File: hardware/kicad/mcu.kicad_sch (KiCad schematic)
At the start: 25 parts, among them J3 JST-XH 2p, SW1 RESET, U3 74LVC1G00, U4 74AHCT1G08, U5 74AHCT1G08

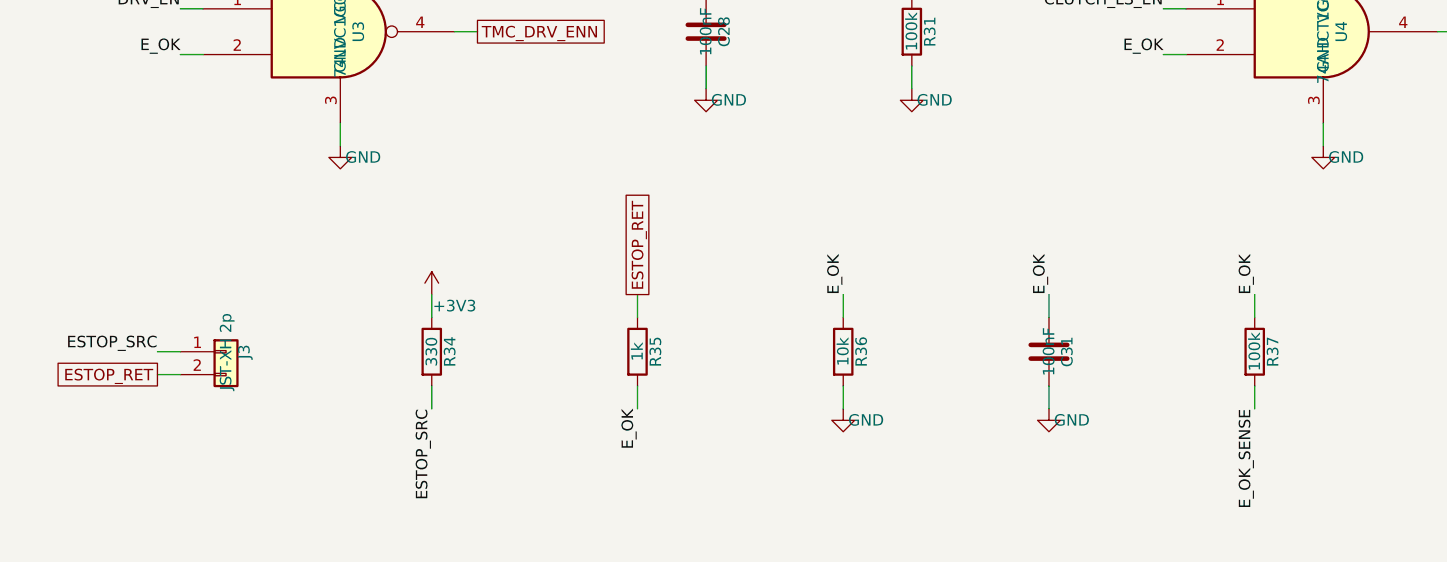
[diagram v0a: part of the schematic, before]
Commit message: Add routed controller PCB, clutch CAD and mill notes
- Schematic: panel ribbon (2x7 IDC) + feed-unit header (JST-XH 7) so all
  connectors fit one 100 mm board edge; fix stub-bridging in the generator.
- PCB (hardware/tools/build_pcb.py): 100x100 mm 4-layer board built from the
  netlist - fixed placement for power/connectors, auto-placed passives,
  GND / split +36V/+3V3 inner planes, Freerouting, post-route power pours,
  GND stitching; fix_planes.py drops plane vias for leftovers;
  check_pcb.py runs DRC with schematic parity. 3D renders in hardware/renders.
  Status: 5 unconnected items + 2 starved thermals left for interactive
  routing (see hardware/kicad/drc.json after check_pcb.py).
- mechanical/clutch: parametric build123d model of the DIY tooth clutch
  (field housing, coil, rotor, armature, leaf springs, output hub/shaft,
  cover), STEP/STL export and VTK renders.
- docs/mill.md: SIEG X3.5D research and the measurements still needed.

Co-Authored-By: Claude Opus 5.5 <noreply@anthropic.com>
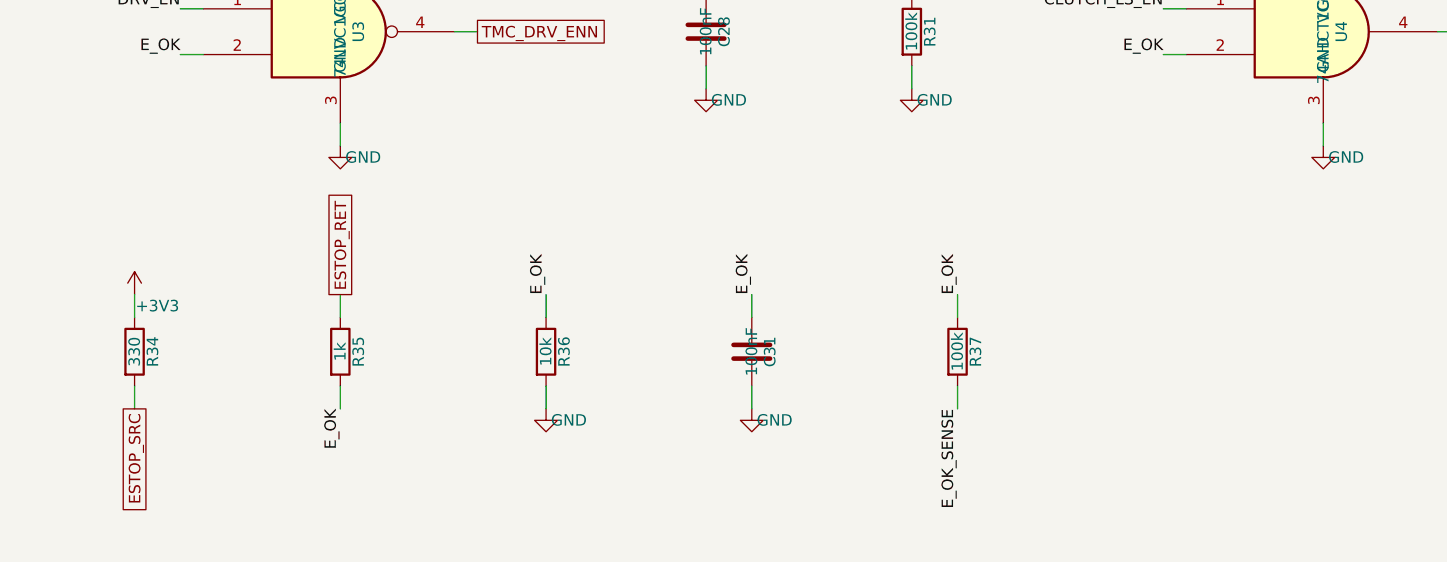
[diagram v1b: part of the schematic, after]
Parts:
- removed J3: JST-XH 2p, Connector_JST:JST_XH_B2B-XH-A_1x02_P2.50mm_Vertical, symbol Connector_Generic:Conn_01x02
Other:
- moved on the sheet: C31, R34, R35, R36, R37

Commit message: Complete LCSC part numbers in the BOM
Every BOM line now has an LCSC number except the Pico module (A1), which
is marked "user-supplied, hand-solder". Parts were checked against the
JLCPCB parts library for spec, Basic/Extended status and stock.

- build_schematic.py: RES_PARTS / CAP_PARTS value+footprint lookup tables
  used by R() / C(), which now raise if a passive has no entry; props for
  the diodes, LEDs, logic ICs, PTC (Littelfuse 2920L050DR, 60 V), IDC
  header (ZHOURI DC3-2.54-14PAS), JST-XH 7p and the Omron B3S-1000 reset
  button.
- Regenerated the schematic sheets, kicad/bom.csv, fab BOM and the README
  missing-LCSC table. PCB, CPL, gerbers and drills are unchanged.

Co-Authored-By: Claude Sonnet 5.5 <noreply@anthropic.com>
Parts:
- A1: MPN (none) -> user-supplied, hand-solder
- C28, C29, C30, C31: LCSC (none) -> C14663; MPN (none) -> Yageo CC0603KRX7R9BB104
- D4: LCSC (none) -> C8598; MPN B5819W -> Changjing B5819W SL
- R24, R25, R26, R27: LCSC (none) -> C23140; MPN (none) -> UNI-ROYAL 0603WAF330JT5E
- R28, R29, R30, R36: LCSC (none) -> C25804; MPN (none) -> UNI-ROYAL 0603WAF1002T5E
- R31, R32, R33, R37: LCSC (none) -> C25803; MPN (none) -> UNI-ROYAL 0603WAF1003T5E
- R34: LCSC (none) -> C23138; MPN (none) -> UNI-ROYAL 0603WAF3300T5E
- R35: LCSC (none) -> C21190; MPN (none) -> UNI-ROYAL 0603WAF1001T5E
- SW1: LCSC (none) -> C2733655; MPN (none) -> Omron B3S-1000
- U3: LCSC (none) -> C7826
- U4, U5: LCSC (none) -> C113521

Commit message: Schematic: bare RP2040 instead of the Pico module
RP2040 (QFN-56) per Raspberry Pi's minimal design: W25Q16JV 2 MB QSPI flash, 12 MHz crystal with 1k series,
internal 1.1 V core regulator, BOOTSEL + RESET buttons, JST-SH SWD, status LED on GPIO25, USB-C (5.1k CC,
27R series). +3V3 now from an AP2112K-3.3 fed by VSYS = +5V or USB VBUS through Schottkys. Same GPIO
numbers as the Pico, so the firmware is unchanged. ERC 0 findings, netlist 132 nets / 189 parts match.
Layout follows (PCB agent). LCSC numbers for the flash and crystal still to be verified.

Co-Authored-By: Claude Opus 5.5 <noreply@anthropic.com>
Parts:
- removed A1: Raspberry Pi Pico, Module:RaspberryPi_Pico_SMD, symbol MCU_Module:RaspberryPi_Pico
- added C32, C33, C34, C35, C38, C39, C40, C45, C46, C47, C48: 100nF, Capacitor_SMD:C_0603_1608Metric, symbol Device:C
- added C36, C37, C43: 1uF, Capacitor_SMD:C_0603_1608Metric, symbol Device:C
- added C41, C42: 15pF, Capacitor_SMD:C_0603_1608Metric, symbol Device:C
- added C44: 4.7uF 10V, Capacitor_SMD:C_0805_2012Metric, symbol Device:C
- added D5, D6: B5819W, Diode_SMD:D_SOD-123, symbol Device:D_Schottky
- added J3: SWD, Connector_JST:JST_SH_SM03B-SRSS-TB_1x03-1MP_P1.00mm_Horizontal, symbol Connector_Generic:Conn_01x03
- added J4: USB-C, Connector_USB:USB_C_Receptacle_HRO_TYPE-C-31-M-12, symbol Connector:USB_C_Receptacle_USB2.0_16P
- added R38, R39, R45: 10k, Resistor_SMD:R_0603_1608Metric, symbol Device:R
- added R40, R41, R42, R46: 100k, Resistor_SMD:R_0603_1608Metric, symbol Device:R
- added R43: 330, Resistor_SMD:R_0603_1608Metric, symbol Device:R
- added R44: 1k, Resistor_SMD:R_0603_1608Metric, symbol Device:R
- added SW2: RESET, Button_Switch_SMD:SW_SPST_B3S-1000, symbol Switch:SW_Push
- added U6: 74LVC1G00, Package_TO_SOT_SMD:SOT-23-5, symbol 74xGxx:74LVC1G00
- added U7, U8: 74AHCT1G08, Package_TO_SOT_SMD:SOT-23-5, symbol 74xGxx:74AHCT1G08
- added Y1: 12MHz, Crystal:Crystal_SMD_3225-4Pin_3.2x2.5mm, symbol Device:Crystal_GND24
- D4: value B5819W -> green; footprint Diode_SMD:D_SOD-123 -> LED_SMD:LED_0603_1608Metric; symbol Device:D_Schottky -> Device:LED; LCSC C8598 -> C12624; MPN Changjing B5819W SL -> KENTO KT-0603G
- R24, R27: value 33 -> 10k; LCSC C23140 -> C25804; MPN UNI-ROYAL 0603WAF330JT5E -> UNI-ROYAL 0603WAF1002T5E
- R25, R26: value 33 -> 1k; LCSC C23140 -> C21190; MPN UNI-ROYAL 0603WAF330JT5E -> UNI-ROYAL 0603WAF1001T5E
- R28: value 10k -> 1k; LCSC C25804 -> C21190; MPN UNI-ROYAL 0603WAF1002T5E -> UNI-ROYAL 0603WAF1001T5E
- R29, R30: value 10k -> 5.1k; LCSC C25804 -> C23186; MPN UNI-ROYAL 0603WAF1002T5E -> UNI-ROYAL 0603WAF5101T5E
- R31, R32: value 100k -> 27; LCSC C25803 -> C25190; MPN UNI-ROYAL 0603WAF1003T5E -> UNI-ROYAL 0603WAF270JT5E
- R33: value 100k -> 33; LCSC C25803 -> C23140; MPN UNI-ROYAL 0603WAF1003T5E -> UNI-ROYAL 0603WAF330JT5E
- R34: value 330 -> 33; LCSC C23138 -> C23140; MPN UNI-ROYAL 0603WAF3300T5E -> UNI-ROYAL 0603WAF330JT5E
- R35: value 1k -> 33; LCSC C21190 -> C23140; MPN UNI-ROYAL 0603WAF1001T5E -> UNI-ROYAL 0603WAF330JT5E
- R36: value 10k -> 33; LCSC C25804 -> C23140; MPN UNI-ROYAL 0603WAF1002T5E -> UNI-ROYAL 0603WAF330JT5E
- R37: value 100k -> 10k; LCSC C25803 -> C25804; MPN UNI-ROYAL 0603WAF1003T5E -> UNI-ROYAL 0603WAF1002T5E
- SW1: value RESET -> BOOTSEL
- U3: value 74LVC1G00 -> RP2040; footprint Package_TO_SOT_SMD:SOT-23-5 -> Package_DFN_QFN:QFN-56-1EP_7x7mm_P0.4mm_EP3.2x3.2mm_ThermalVias; symbol 74xGxx:74LVC1G00 -> MCU_RaspberryPi:RP2040; LCSC C7826 -> C2040; MPN SN74LVC1G00DBVR -> Raspberry Pi RP2040
- U4: value 74AHCT1G08 -> W25Q16JVSS; footprint Package_TO_SOT_SMD:SOT-23-5 -> Package_SO:SOIC-8_5.3x5.3mm_P1.27mm; symbol 74xGxx:74AHCT1G08 -> Memory_Flash:W25Q16JVSS; LCSC C113521 -> (none); MPN SN74AHCT1G08DBVR -> Winbond W25Q16JVSSIQ
- U5: value 74AHCT1G08 -> AP2112K-3.3; symbol 74xGxx:74AHCT1G08 -> Regulator_Linear:AP2112K-3.3; LCSC C113521 -> C51118; MPN SN74AHCT1G08DBVR -> Diodes AP2112K-3.3TRG1
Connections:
- net +3V3: now also C29.1, C30.1, C31.1, R24.2, R27.2, R37.2, U3.1 (IOVDD), U3.10 (IOVDD), U3.22 (IOVDD), U3.33 (IOVDD), U3.42 (IOVDD), U3.43 (ADC_AVDD), U3.44 (VREG_VIN), U3.48 (USB_VDD), U3.49 (IOVDD), U4.8 (VCC), U5.5 (VOUT), C32.1, C33.1, C34.1, C35.1, C36.1, C40.1, C44.1, C45.1, R38.2, R39.2, R43.1, U6.5 (VCC); no longer R28.2, R29.2, R30.2, R34.1, U3.5 (VCC)
- net +5V: now also C46.1, C47.1, D5.2 (A), U7.5 (VCC), U8.5 (VCC); no longer C29.1, C30.1, D4.2 (A), U4.5 (VCC), U5.5 (VCC)
- net CLUTCH_HS_DRV: now also U8.4; no longer U5.4
- net CLUTCH_HS_PWM: now also U3.4 (GPIO2), R42.1, U8.1; no longer R33.1, U5.1
- net CLUTCH_ISENSE: now also U3.39 (GPIO27/ADC1)
- net CLUTCH_LS_EN: now also U3.11 (GPIO8), R41.1, U7.1; no longer R32.1, U4.1
- net CLUTCH_LS_GATE: now also U7.4; no longer U4.4
- net DIAL_A: now also U3.13 (GPIO10)
- net DIAL_B: now also U3.14 (GPIO11)
- net DIAL_SW: now also U3.15 (GPIO12)
- net DRV_EN: now also U3.31 (GPIO20), R40.1, U6.1; no longer R31.1, U3.1
- net ENC_OUT_A: now also U3.2 (GPIO0)
- net ENC_OUT_B: now also U3.3 (GPIO1)
- net ESTOP_RET: now also R44.1; no longer R35.1
- net ESTOP_SRC: now also R43.2; no longer R34.2
- net E_OK: now also C48.1, R44.2, R45.1, R46.1, U6.2, U7.2, U8.2; no longer C31.1, R35.2, R36.1, R37.1, U3.2, U4.2, U5.2
- net E_OK_SENSE: now also U3.5 (GPIO3), R46.2; no longer R37.2
- net GND: now also D4.1 (K), R29.2, R30.2, U3.19 (TESTEN), U3.57 (GND), U4.4 (GND), U5.2 (GND), C32.2, C33.2, C34.2, C35.2, C36.2, C37.2, C38.2, C39.2, C40.2, C41.2, C42.2, C43.2, C44.2, C45.2, C46.2, C47.2, C48.2, J3.2 (Pin_2), J4.A1 (GND), J4.A12 (GND), J4.B1 (GND), J4.B12 (GND), J4.S1 (SHIELD), R40.2, R41.2, R42.2, R45.2, SW2.2, U6.3 (GND), U7.3 (GND), U8.3 (GND), Y1.2 (G), Y1.4 (G); no longer R31.2, R32.2, R33.2, R36.2, U3.3 (GND), U4.3 (GND), U5.3 (GND)
- net I2C_SCL: now also U3.7 (GPIO5)
- net I2C_SDA: now also U3.6 (GPIO4)
- net LIM_L: now also U3.8 (GPIO6)
- net LIM_R: now also U3.9 (GPIO7)
- net MODE_L: now also U3.16 (GPIO13)
- net MODE_R: now also U3.17 (GPIO14)
- net RAPID: now also U3.18 (GPIO15)
- net RUN: now also R27.1, U3.26 (RUN), SW2.1; no longer SW1.1
- net SPI_CS: now also R35.1, U3.28 (GPIO17); no longer R26.1
- net SPI_MISO: now also R36.2, U3.27 (GPIO16); no longer R27.2
- net SPI_MOSI: now also R34.1, U3.30 (GPIO19); no longer R25.1
- net SPI_SCK: now also R33.1, U3.29 (GPIO18); no longer R24.1
- net TMC_CSN: now also R35.2, R37.1; no longer R26.2, R28.1
- net TMC_DIAG0: now also U3.32 (GPIO21), R38.1; no longer R29.1
- net TMC_DIAG1: now also U3.34 (GPIO22), R39.1; no longer R30.1
- net TMC_DRV_ENN: now also U6.4; no longer U3.4
- net TMC_SCK: now also R33.2; no longer R24.2
- net TMC_SDI: now also R34.2; no longer R25.2
- net TMC_SDO: now also R36.1; no longer R27.1
- net VM_SENSE: now also U3.38 (GPIO26/ADC0)
- net VSYS: now also U5.1 (VIN), U5.3 (EN), C43.1, D5.1 (K), D6.1 (K); no longer D4.1 (K)
- new net BOOTSEL_SW: R25.2, SW1.1
- new net LED_STAT: R28.1, U3.37 (GPIO25)
- new net LED_STAT_A: D4.2 (A), R28.2
- new net QSPI_SCLK: U3.52 (QSPI_SCLK), U4.6 (CLK)
- new net QSPI_SD0: U3.53 (QSPI_SD0), U4.5 (DI/IO_{0})
- new net QSPI_SD1: U3.55 (QSPI_SD1), U4.2 (DO/IO_{1})
- new net QSPI_SD2: U3.54 (QSPI_SD2), U4.3 (~{WP}/IO_{2})
- new net QSPI_SD3: U3.51 (QSPI_SD3), U4.7 (~{HOLD}/~{RESET}/IO_{3})
- new net QSPI_SS: R24.1, R25.1, U3.56 (~{QSPI_SS}), U4.1 (~{CS})
- new net SWCLK: J3.1 (Pin_1), U3.24 (SWCLK)
- new net SWDIO: J3.3 (Pin_3), U3.25 (SWDIO)
- new net USB_CC1: J4.A5 (CC1), R29.1
- new net USB_CC2: J4.B5 (CC2), R30.1
- new net USB_CONN_DM: J4.A7 (D-), J4.B7 (D-), R32.1
- new net USB_CONN_DP: J4.A6 (D+), J4.B6 (D+), R31.1
- new net USB_DM: R32.2, U3.46 (USB_DM)
- new net USB_DP: R31.2, U3.47 (USB_DP)
- new net VBUS: D6.2 (A), J4.A4 (VBUS), J4.A9 (VBUS), J4.B4 (VBUS), J4.B9 (VBUS)
- new net VDD_CORE: C37.1, C38.1, C39.1, U3.23 (DVDD), U3.45 (VREG_VOUT), U3.50 (DVDD)
- new net XIN: C41.1, U3.20 (XIN), Y1.1
- new net XOUT: R26.1, U3.21 (XOUT)
- new net XTAL_OUT: C42.1, R26.2, Y1.3
- no-connect marks 5 -> 8
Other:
- note added: "Interlock (hardware, independent of firmware): TMC_DRV_ENN = NAND(DRV_EN, E_OK) -> driver off unless the MCU enables it AND E-stop loop closed CLUTCH_* = AND(MCU request, E_OK) -> clutch off on E-stop MCU outputs have pull-downs so everything is off while the RP2040 is in reset. E-stop: NC contact between ESTOP_SRC (+3V3 via 330R) and ESTOP_RET. Open or broken wire -> E_OK low. The MCU only reads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"
- note removed: "Interlock (hardware, independent of firmware): TMC_DRV_ENN = NAND(DRV_EN, E_OK) -> driver off unless Pico enables it AND E-stop loop closed CLUTCH_* = AND(Pico request, E_OK) -> clutch off on E-stop Pico outputs have pull-downs so everything is off while the Pico is in reset. E-stop: NC contact between ESTOP_SRC (+3V3 via 330R) and ESTOP_RET. Open or broken wire -> E_OK low. The Pico only reads E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"
- title: Pico, SPI, E-stop interlock -> RP2040, SPI, E-stop interlock
- moved on the sheet: C28, C29, C30, C31, R24, R25, R26, R27, R28, R29, R30, R31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
